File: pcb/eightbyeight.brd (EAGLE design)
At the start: 60 x 60 mm, 131 parts, among them CON1 USB_MICROSMT+THRUHULE, Q1 16MHz, SW1 SWITCH_SPDT, SW2 BRIGHTNESS, U1 MK20D--VFM5, U2 ICN2026, U3 74138, U4 ICN2026, U5 MIC5219 3.3V, U8 MMA8653FC

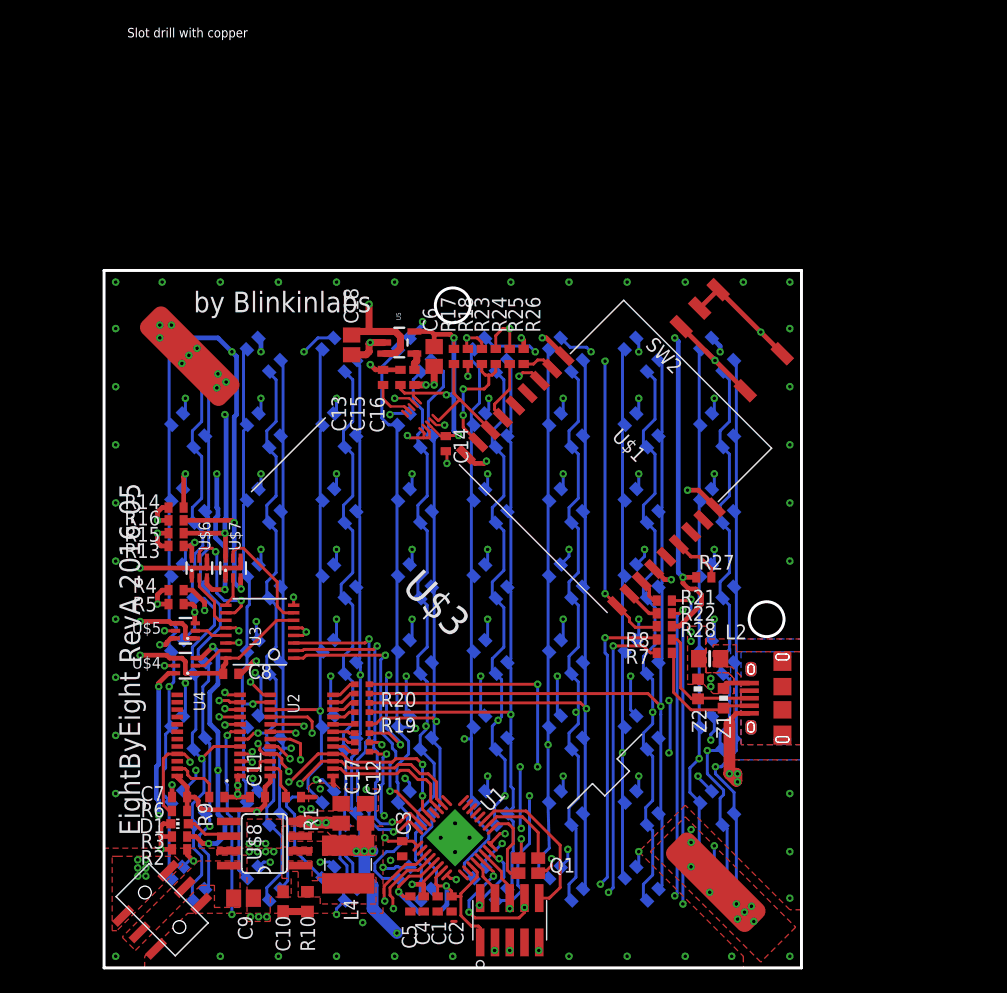
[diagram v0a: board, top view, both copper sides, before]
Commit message: Clean up label placements on PCB
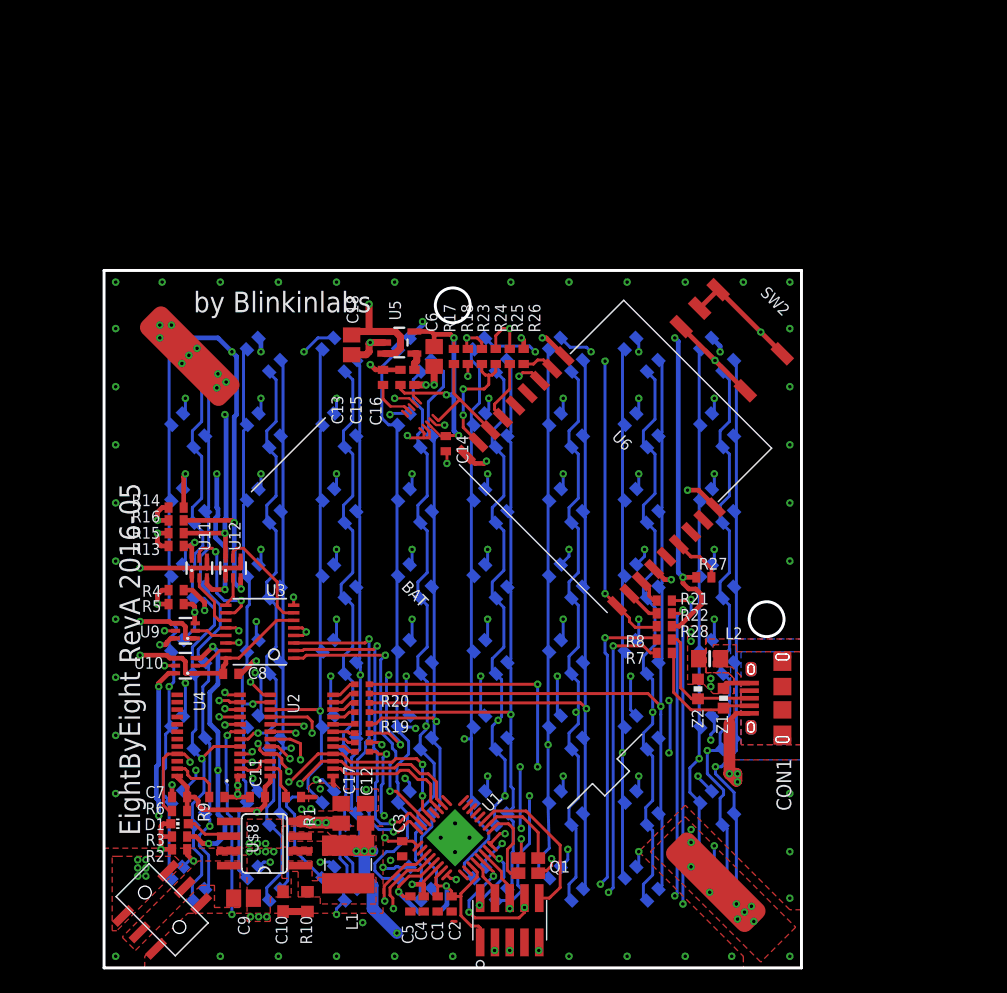
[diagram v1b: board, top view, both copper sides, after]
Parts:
- renumbered L4 to L1, U$1 to U6, U$3 to BAT, U$4 to U10, U$5 to U9, U$6 to U11, U$7 to U12
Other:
- board text removed: "3V3"
- board text removed: "5V"
- board text removed: "GND"
- board text removed: "LeoBlinky 2015 Created with love by Blinkinlabs"
- board text removed: "RST"
- board text removed: "RX"
- board text removed: "Slot drill with copper"
- board text removed: "TCK"
- board text removed: "TMS"
- board text removed: "TX"

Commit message: Routing changes on PCB, cleanup
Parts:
- removed R24: DNP, adafruit:R0402
- added D2, D3: RB161M-20, adafruit:SOD-123
- added R11: 50, adafruit:R0805
- U1: value MK20D--VFM5 -> MK20DN64VFM5
- moved C14 0.10 mm to (29.3, 45.1)
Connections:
- net N$8 renamed ESP_ENABLE
- removed net N$11: R27.1, U6.RST
- new net BOOST_5V: C9.1, D2.A, U$8.8
- new net ESP_RESET: R27.1, U1.20, U6.RST
- new net N$1: D2.C, D3.C, SW1.S0, SW1.S1
- net +5V: now also SW1.P0, SW1.P1; no longer SW1.S0, SW1.S1
- net ESP_GPIO0: now also U1.21; no longer R24.2
- net GND: now also R11.1; no longer R24.1
- net N$4: now also R11.2, SW1.O0, SW1.O1; no longer C9.1, SW1.P0, SW1.P1, U$8.8
- net USB_5V: now also D3.A
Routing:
- net ESP_RESET: track 0.00 -> 47.8 mm, vias 0 -> 3
- net ESP_GPIO0: track 11.0 -> 44.7 mm, vias 2 -> 3
- net N$11: track 4.42 -> 0.00 mm
- net GND: track 88.6 -> 86.0 mm
- net ARM_3V3: track 60.4 -> 62.0 mm
- net +3V3: track 77.5 -> 76.9 mm
- added copper zone on layer 1, net BOOST_5V
- removed copper zone on layer 1, net N$4
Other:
- board text added: "EightByEight RevB 2016-06"
- board text removed: "EightByEight RevA 2016-05"

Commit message: Continue implementing changes from TODO
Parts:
- removed R21, R22: 0, adafruit:R0402
- added ANALOG_IN, TP1, TP2, TP3: PTR1B2,54, testpad:B2,54
- added R12: 10k, adafruit:R0402
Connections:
- removed net ESP_RXD: R22.1, U6.RXD
- removed net ESP_TXD: R21.1, U6.TXD
- removed net I2C_SDA: R17.1, U6.IO2, U8.P$10
- new net ARM_RX1: R12.1, R17.1, U1.24, U6.IO2, U8.P$10
- new net ESP_EXP_1: TP3.TP, U6.IO5
- new net ESP_EXP_2: TP2.TP, U6.IO12
- new net ESP_EXP_3: TP1.TP, U6.IO18
- new net ESP_TOUT: ANALOG_IN.TP, U6.TOUT
- net +3V3: now also R12.2
- net ACC_INT1: now also U6.IO13
- net ARM_RX: now also U6.TXD; no longer R21.2
- net ARM_TX: now also U6.RXD; no longer R22.2
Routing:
- net ARM_RX1: track 0.00 -> 48.9 mm, vias 0 -> 2
- net I2C_SDA: track 9.95 -> 0.00 mm
- net ARM_TX: track 46.3 -> 49.4 mm
- net ESP_RXD: track 3.05 -> 0.00 mm
- net ESP_TXD: track 2.33 -> 0.00 mm
- net ARM_RX: track 54.3 -> 56.0 mm
- net BCOL4: track 68.6 -> 69.3 mm
- net +3V3: track 76.9 -> 77.4 mm

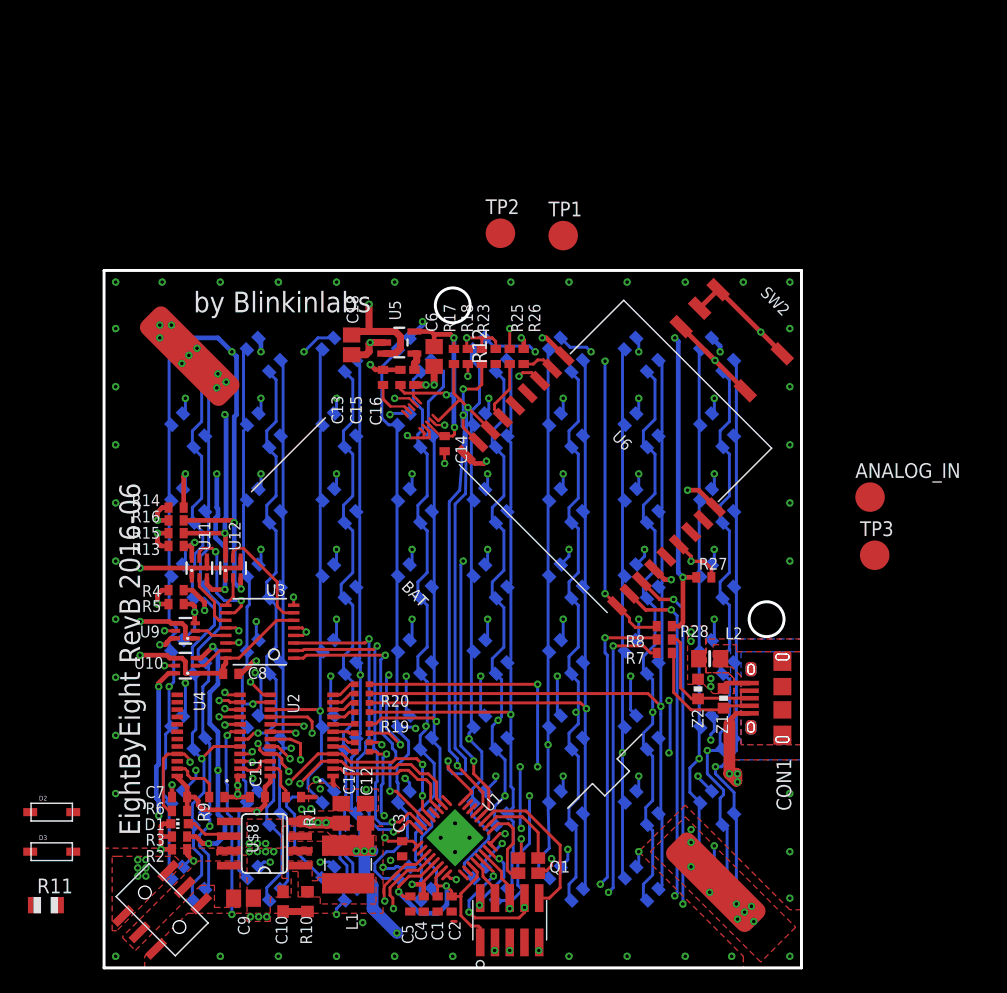
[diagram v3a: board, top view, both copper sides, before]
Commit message: Finish routing accelerometer changes
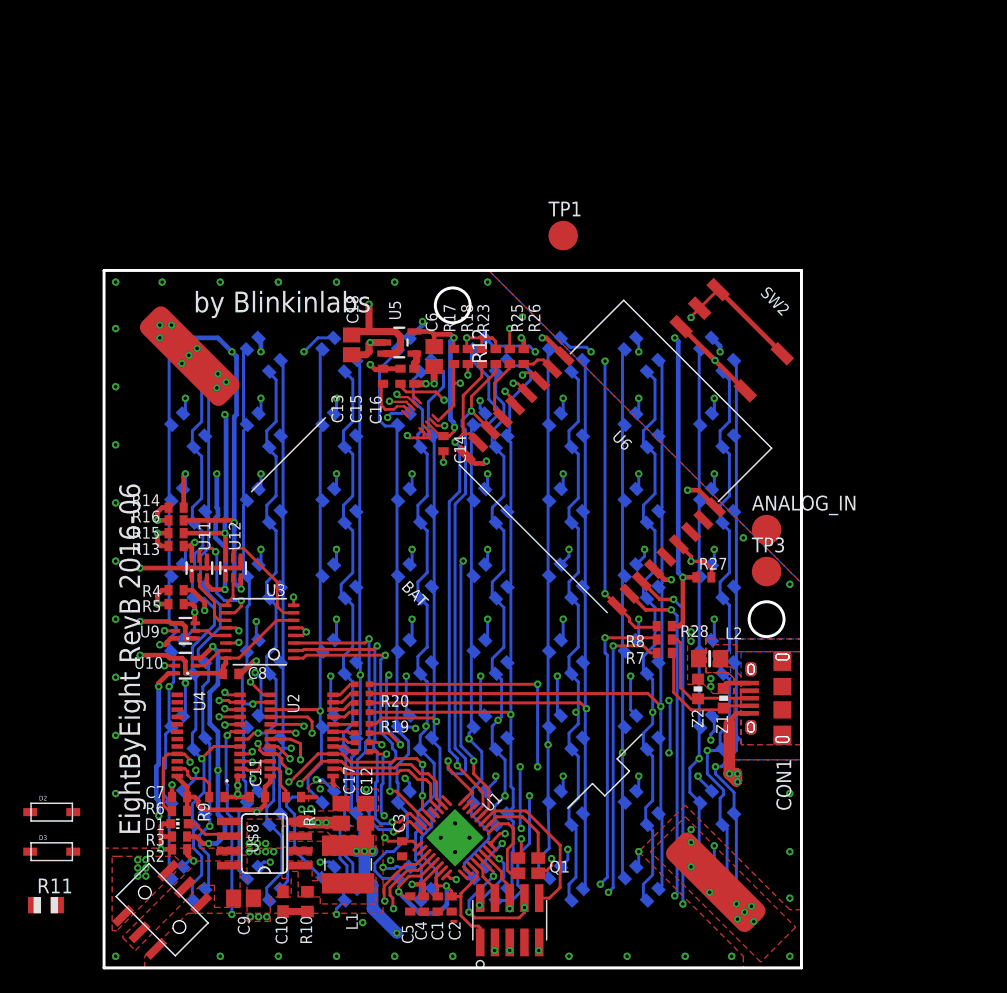
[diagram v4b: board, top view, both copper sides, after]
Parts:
- removed TP2: PTR1B2,54, testpad:B2,54
- moved TP3 9.40 mm to (57.0, 34.1)
- moved ANALOG_IN 9.33 mm to (57.0, 37.7)
- moved C13 0.10 mm to (24.0, 50.9)
- moved C14 0.10 mm to (29.2, 45.1)
- moved C15 0.10 mm to (25.5, 50.9)
- moved C16 0.10 mm to (26.7, 50.9)
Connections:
- removed net ESP_EXP_2: TP2.TP, U6.IO12
- new net I2C_SDA: R17.1, U6.IO12, U8.P$10
- net ARM_RX1: no longer R17.1, U8.P$10
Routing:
- net GND: track 86.0 -> 100.4 mm, vias 97 -> 90
- net ACC_INT1: track 0.00 -> 14.2 mm, vias 0 -> 2
- net I2C_SDA: track 0.00 -> 12.5 mm, vias 0 -> 2
- net ARM_RX1: track 48.9 -> 46.3 mm
- net RCOL4: track 59.8 -> 61.8 mm
- net BCOL4: track 69.3 -> 71.1 mm
- net ESP_GPIO0: track 44.8 -> 43.1 mm, vias 3 -> 2
- net N$5: track 3.78 -> 4.61 mm
- net I2C_SCL: track 16.7 -> 16.2 mm

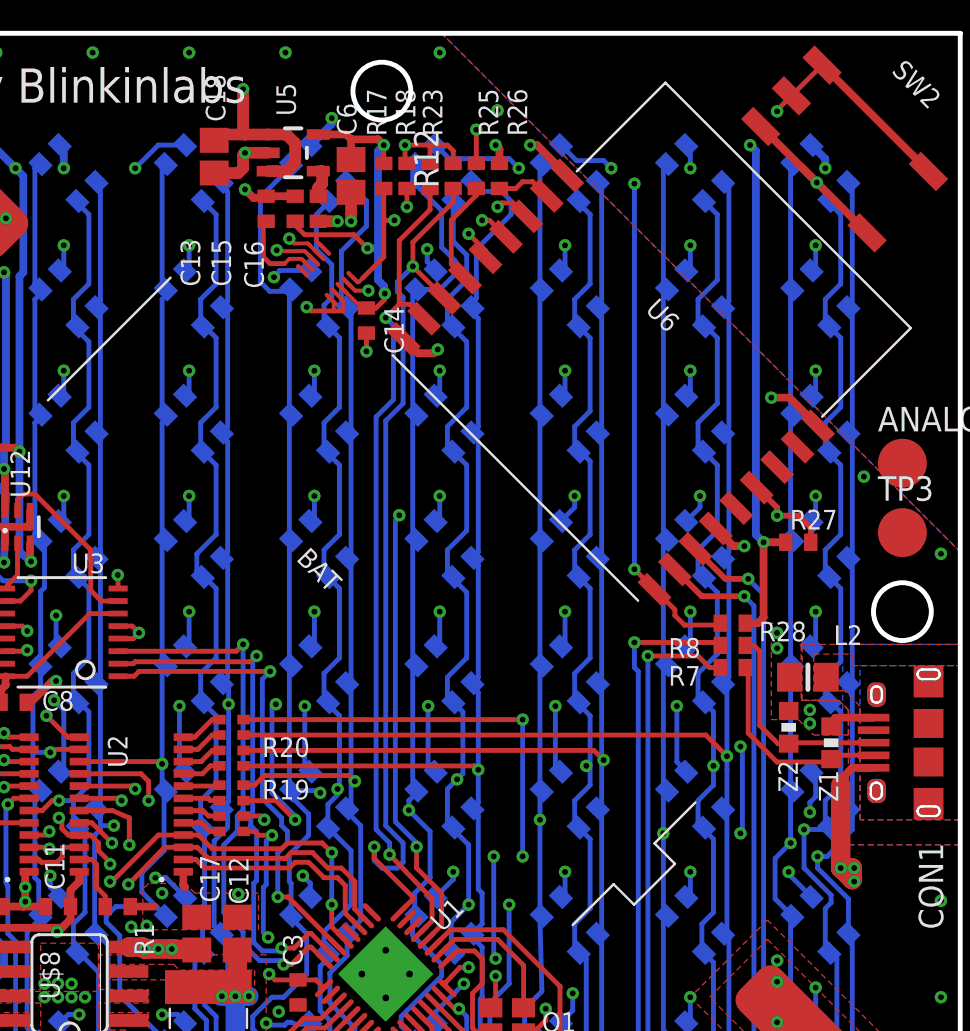
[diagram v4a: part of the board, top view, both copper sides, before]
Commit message: PCB: Add LED_OE to row driver mux enable
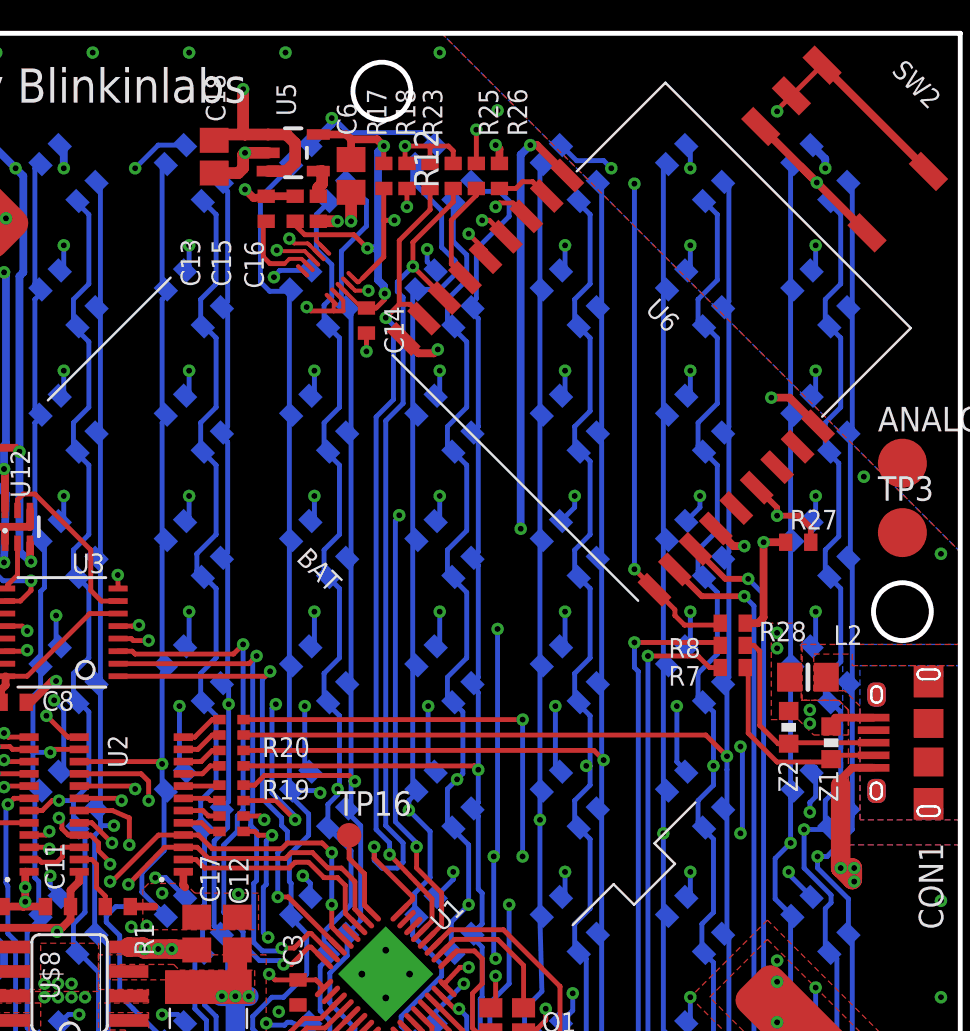
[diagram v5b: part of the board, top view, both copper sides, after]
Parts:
- added TP16: PTR1B1,27, testpad:B1,27
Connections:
- new net ARM_BOOTLOADER: TP16.TP, U1.25
- net GND: no longer U3.4
- net LED_OE: now also U3.4
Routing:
- net LED_OE: track 48.8 -> 80.6 mm, vias 6 -> 8
- net ARM_BOOTLOADER: track 0.00 -> 4.49 mm
- net GND: track 100.4 -> 99.0 mm
- net 1ROW7: track 92.6 -> 93.8 mm, vias 10 -> 9
- net +3V3: track 77.4 -> 78.0 mm

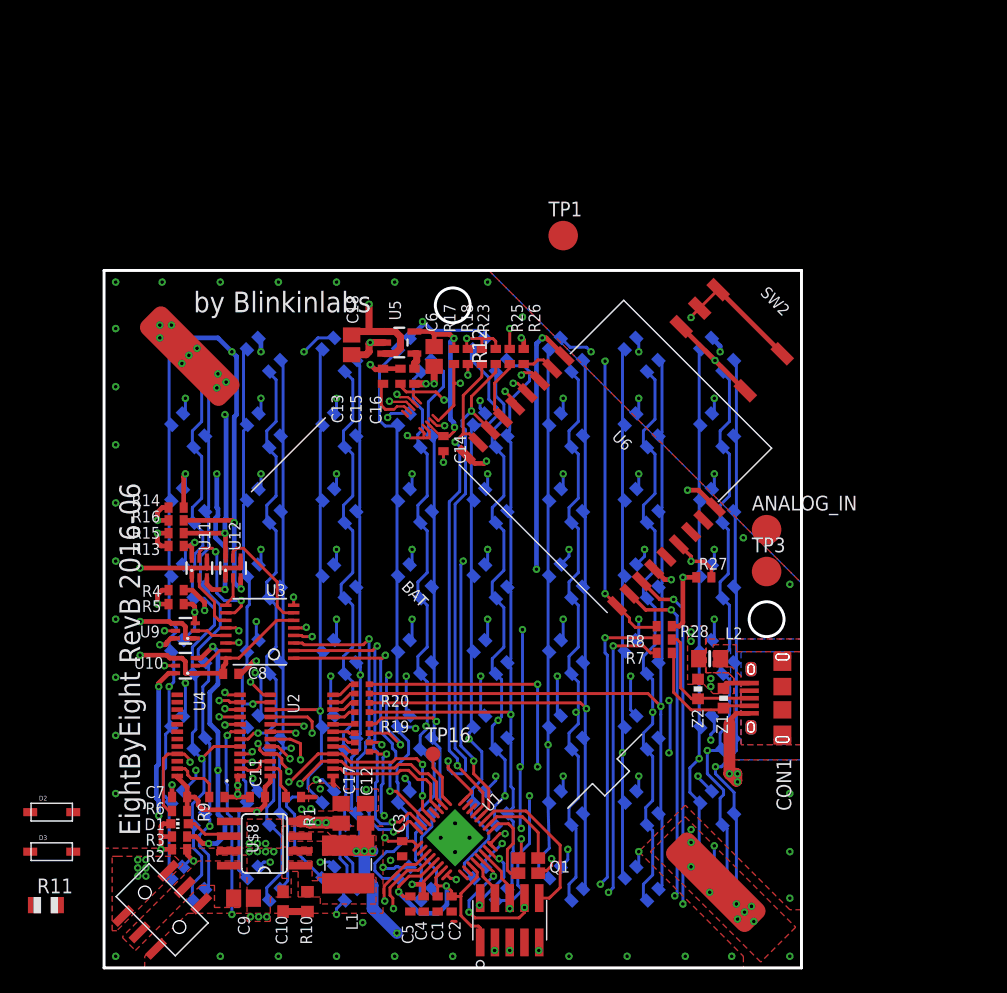
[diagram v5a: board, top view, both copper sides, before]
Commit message: Add LED_HS_EN. Increase number of vias on power lines
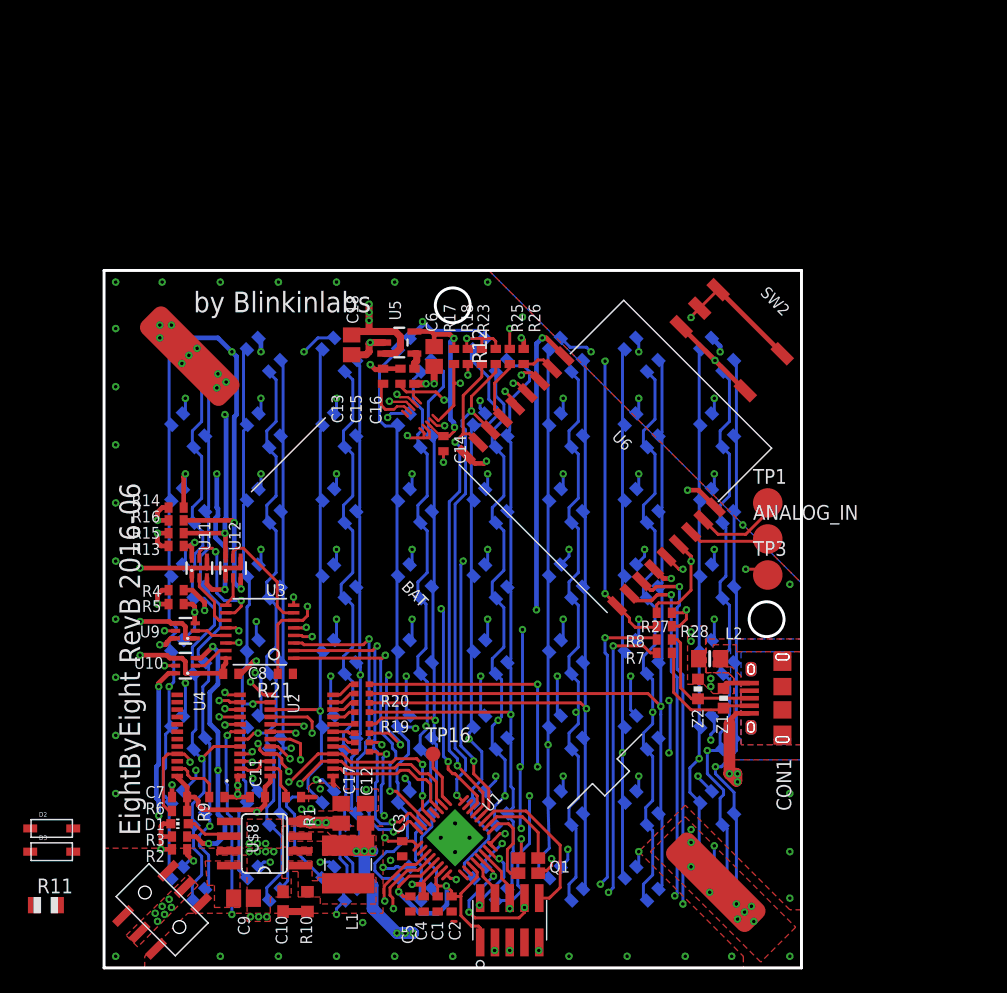
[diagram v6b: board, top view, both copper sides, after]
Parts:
- added R21: 2k 1%, adafruit:R0402
- moved TP1 29.0 mm to (57.1, 40.0)
- moved R27 4.57 mm to (48.2, 30.6), turned to 0 degrees
- moved D2 1.40 mm to (-4.50, 12.0)
- moved ANALOG_IN 0.81 mm to (57.1, 36.9)
- moved TP3 0.32 mm to (57.1, 33.8)
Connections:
- net ESP_EXP_3 renamed ESP_EXP_2
- new net LED_HS_EN: R21.2, U1.22, U3.6
- net +5V: no longer U3.6
- net GND: now also R21.1
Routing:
- net LED_HS_EN: track 0.00 -> 38.3 mm, vias 0 -> 3
- net ESP_EXP_1: track 0.00 -> 9.37 mm, vias 0 -> 2
- net ESP_EXP_2: track 0.00 -> 7.84 mm
- net ESP_TOUT: track 0.00 -> 7.15 mm
- net +5V: track 143.4 -> 138.9 mm, vias 11 -> 13
- net ESP_RESET: track 47.7 -> 51.6 mm
- net ARM_RX1: track 46.3 -> 42.6 mm
- net VBAT: track 42.7 -> 44.8 mm, vias 13 -> 15
- net ARM_RX: track 56.0 -> 57.4 mm
- net ARM_TX: track 49.4 -> 50.6 mm
- net +3V3: track 78.0 -> 79.0 mm
- net RCOL3: track 55.2 -> 54.6 mm
- added copper zone on layer 15, net +5V
